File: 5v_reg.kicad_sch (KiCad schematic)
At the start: 33 parts, among them U3 SIC461ED-T1-GE3

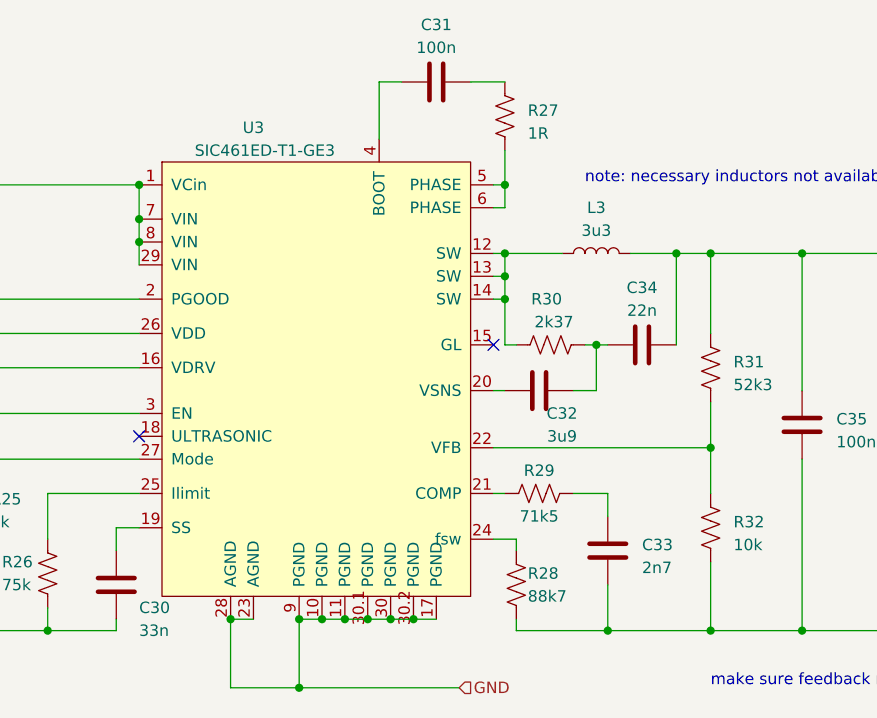
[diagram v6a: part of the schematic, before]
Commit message: drc fixes and update schematic to reflect correct ic footprints
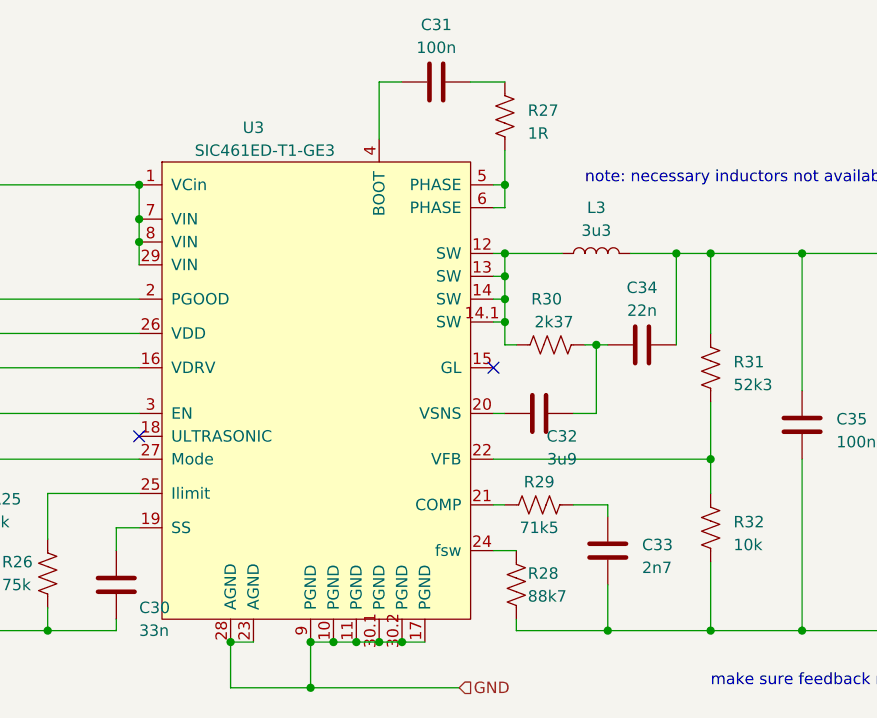
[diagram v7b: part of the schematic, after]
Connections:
- net GND: no longer U3.30 (PGND)
- net at L3.1, R30.1, U3.12 (SW)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: now also U3.14.1 (SW)
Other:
- moved on the sheet: C32, R29, U3

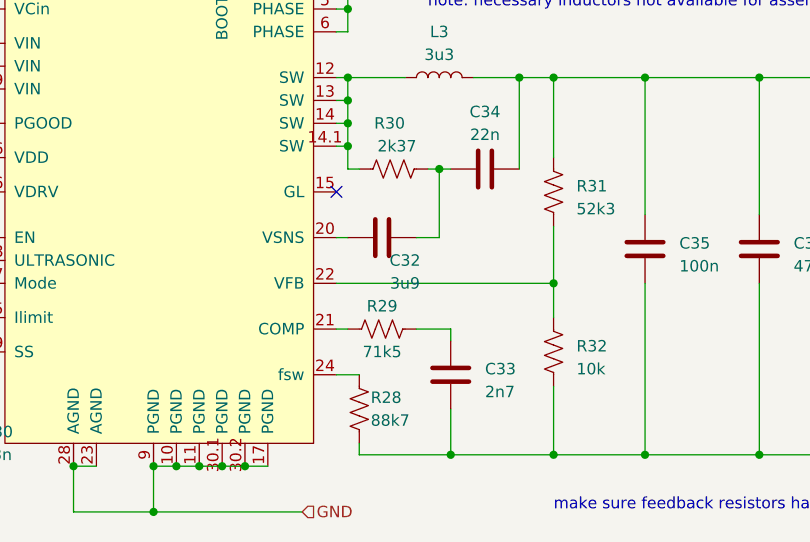
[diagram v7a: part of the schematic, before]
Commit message: use 4u7 capacitors for vsns pins
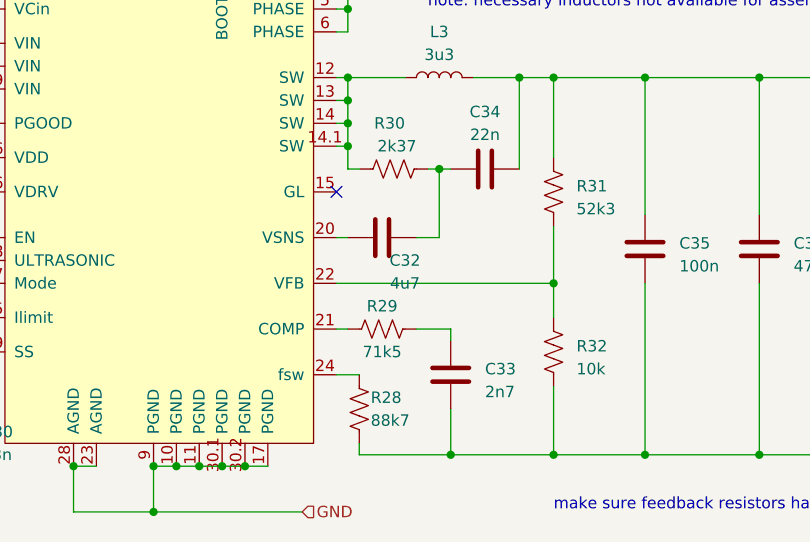
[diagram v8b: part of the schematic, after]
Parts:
- C32: value 3u9 -> 4u7; footprint Capacitor_SMD:C_0402_1005Metric -> Capacitor_SMD:C_0805_2012Metric
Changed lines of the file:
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@@
       (effects (font (size 1.27 1.27)))
     )
-    (property "Value" "3u9" (at 147.32 107.95 90)
+    (property "Value" "4u7" (at 147.32 107.95 90)
       (effects (font (size 1.27 1.27)))
     )
-    (property "Footprint" "Capacitor_SMD:C_0402_1005Metric" (at 148.59 101.9048 0)
+    (property "Footprint" "Capacitor_SMD:C_0805_2012Metric" (at 148.59 101.9048 0)
       (effects (font (size 1.27 1.27)) hide)
     )
